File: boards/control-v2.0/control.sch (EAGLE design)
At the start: 107 parts, among them IC1 MCP23017-E/SS, J1 HFW8R-1ST, J2 B2PS-CENTERED-VH(LF)(SN), J3 SBH11-PBPC-D05-RA, J9 DF22-2, U1 TLV70233DBVR, U3 VND5E006ASPTR-E, U4 LMZ14201, U5 MCP1824T-1202E/OT, U6 MCP1824T-2502E/OT, X1 ASV-18.432MHZ-EJ-T

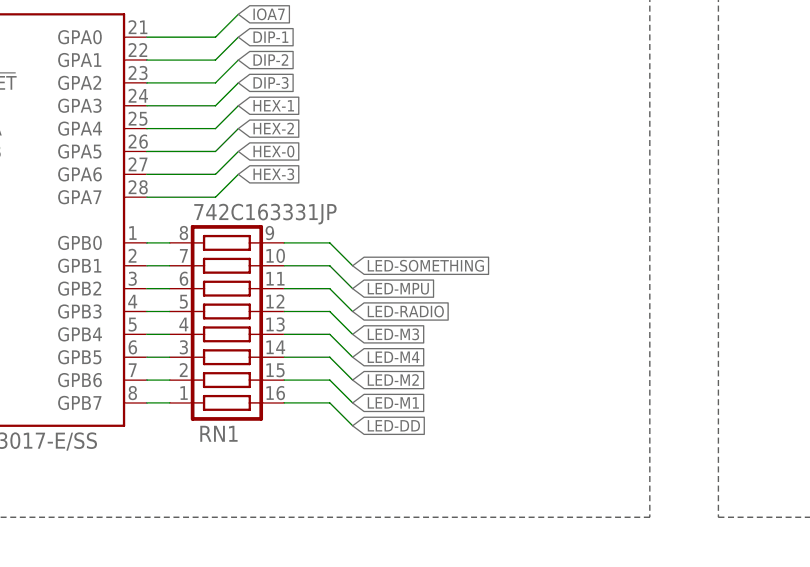
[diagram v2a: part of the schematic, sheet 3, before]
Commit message: Control technically no airwires and passes DRC
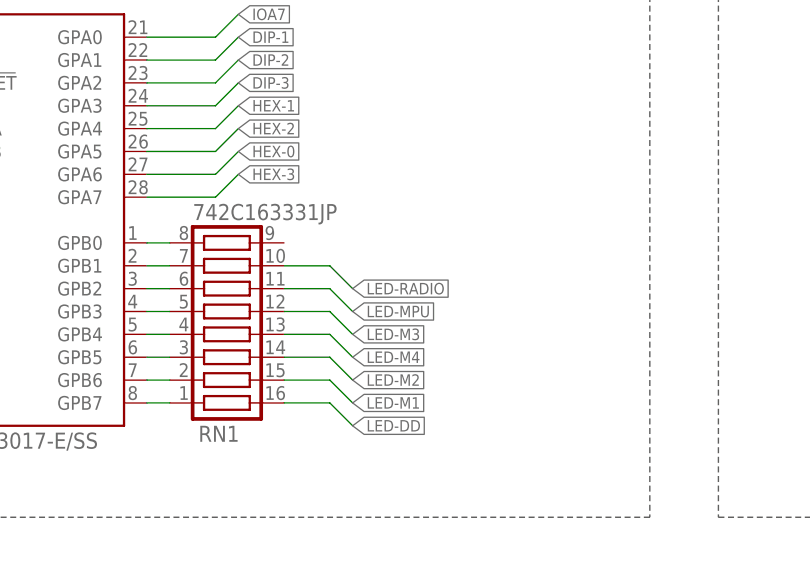
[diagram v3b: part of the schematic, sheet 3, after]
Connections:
- removed net LED-SOMETHING: RN1.9
- net LED-MPU: now also RN1.11; no longer RN1.10
- net LED-RADIO: now also RN1.10; no longer RN1.11
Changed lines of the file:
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@@
 <net name="LED-RADIO" class="0">
+<segment>
+<pinref part="D9" gate="G$1" pin="K"/>
+<wire x1="226.06" y1="172.72" x2="223.52" y2="172.72" width="0.1524" layer="91"/>
+<label x="223.52" y="172.72" size="1.27" layer="95" rot="R180" xref="yes"/>
+</segment>
+<segment>
+<wire x1="93.98" y1="162.56" x2="96.52" y2="160.02" width="0.1524" layer="91"/>
+<label x="96.52" y="160.02" size="1.27" layer="95" xref="yes"/>
+<pinref part="RN1" gate="G$1" pin="10"/>
+<wire x1="88.9" y1="162.56" x2="93.98" y2="162.56" width="0.1524" layer="91"/>
+</segment>
+</net>
+<net name="LED-DD" class="0">
+<segment>
+<wire x1="93.98" y1="147.32" x2="96.52" y2="144.78" width="0.1524" layer="91"/>
+<label x="96.52" y="144.78" size="1.27" layer="95" xref="yes"/>
+<pinref part="RN1" gate="G$1" pin="16"/>
+<wire x1="88.9" y1="147.32" x2="93.98" y2="147.32" width="0.1524" layer="91"/>
+</segment>
+</net>
+<net name="LED-MPU" class="0">
+<segment>
+<pinref part="D10" gate="G$1" pin="K"/>
+<wire x1="38.1" y1="114.3" x2="40.64" y2="114.3" width="0.1524" layer="91"/>
+<label x="40.64" y="114.3" size="1.27" layer="95" xref="yes"/>
+</segment>
 <segment>
 <wire x1="93.98" y1="160.02" x2="96.52" y2="157.48" width="0.1524" layer="91"/>
@@
 <pinref part="RN1" gate="G$1" pin="11"/>
 <wire x1="88.9" y1="160.02" x2="93.98" y2="160.02" width="0.1524" layer="91"/>
-</segment>
-<segment>
-<pinref part="D9" gate="G$1" pin="K"/>
-<wire x1="226.06" y1="172.72" x2="223.52" y2="172.72" width="0.1524" layer="91"/>
-<label x="223.52" y="172.72" size="1.27" layer="95" rot="R180" xref="yes"/>
-</segment>
-</net>
-<net name="LED-DD" class="0">
-<segment>
-<wire x1="93.98" y1="147.32" x2="96.52" y2="144.78" width="0.1524" layer="91"/>
-<label x="96.52" y="144.78" size="1.27" layer="95" xref="yes"/>
-<pinref part="RN1" gate="G$1" pin="16"/>
-<wire x1="88.9" y1="147.32" x2="93.98" y2="147.32" width="0.1524" layer="91"/>
-</segment>
-</net>
-<net name="LED-MPU" class="0">
-<segment>
-<pinref part="D10" gate="G$1" pin="K"/>
-<wire x1="38.1" y1="114.3" x2="40.64" y2="114.3" width="0.1524" layer="91"/>
-<label x="40.64" y="114.3" size="1.27" layer="95" xref="yes"/>
-</segment>
-<segment>
-<wire x1="93.98" y1="162.56" x2="96.52" y2="160.02" width="0.1524" layer="91"/>
-<label x="96.52" y="160.02" size="1.27" layer="95" xref="yes"/>
-<pinref part="RN1" gate="G$1" pin="10"/>
-<wire x1="88.9" y1="162.56" x2="93.98" y2="162.56" width="0.1524" layer="91"/>
 </segment>
 </net>
@@
 </segment>
 </net>
-<net name="LED-SOMETHING" class="0">
-<segment>
-<wire x1="93.98" y1="165.1" x2="96.52" y2="162.56" width="0.1524" layer="91"/>
-<label x="96.52" y="162.56" size="1.27" layer="95" xref="yes"/>
-<pinref part="RN1" gate="G$1" pin="9"/>
-<wire x1="88.9" y1="165.1" x2="93.98" y2="165.1" width="0.1524" layer="91"/>
-</segment>
-</net>

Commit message: Control switch layers, minor changes
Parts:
- SB1, SB2, SB3, SB4: value (none) -> SOLDERBRIDGESB0603
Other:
- moved on the sheet: C16, C17, C18, C19, C20, C21, C22, C23, C24, C25, C26, C27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

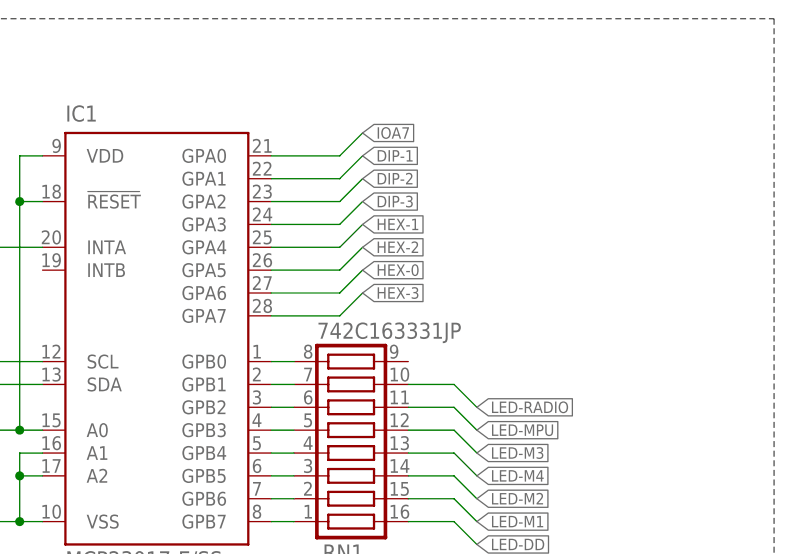
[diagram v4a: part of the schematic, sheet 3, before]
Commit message: Some clean up, smaller board
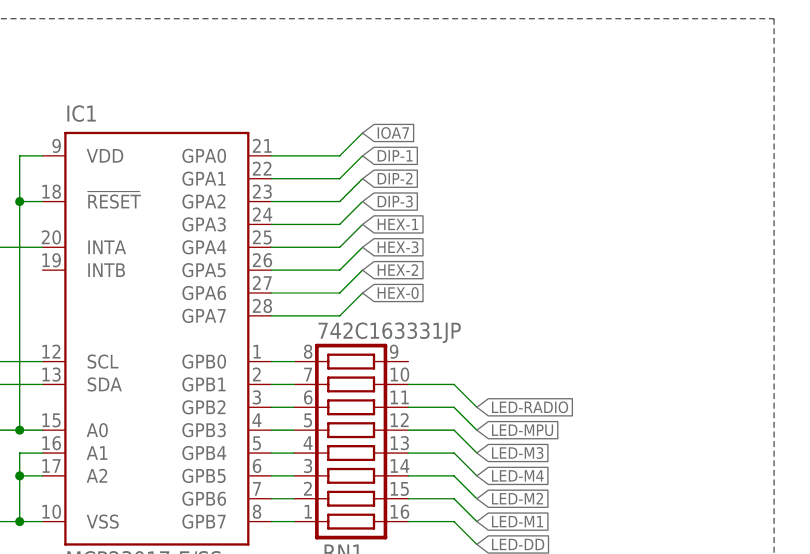
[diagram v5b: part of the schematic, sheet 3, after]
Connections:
- net +5V: now also J2.4; no longer U$1.4
- net ENC-A: now also J2.2; no longer J1G$1.2
- net ENC-B: now also J2.1; no longer J1G$1.1
- net GND: now also J1G$1.2, J2.3; no longer U$1.2
- net H1: now also J1G$1.1; no longer U$1.1
- net H2: now also J1G$1.3; no longer U$1.3
- net H3: now also J1G$1.5; no longer U$1.5
- net HEX-0: now also IC1.GPA7; no longer IC1.GPA6
- net HEX-2: now also IC1.GPA6; no longer IC1.GPA5
- net HEX-3: now also IC1.GPA5; no longer IC1.GPA7
- net PHASE-A: now also J1G$1.7; no longer U$1.7
- net PHASE-B: now also J1G$1.8; no longer U$1.8
- net PHASE-C: no longer U$1.6
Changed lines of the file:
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@@
 <part name="GND12" library="supply1" deviceset="GND" device=""/>
 <part name="SUPPLY1" library="supply2" deviceset="+5V" device=""/>
-<part name="U$1" library="RoboJackets-Connectors" deviceset="MKS-1658" device=""/>
-<part name="J1" library="RoboJackets-Connectors" deviceset="4-PIN_2MM-*" device="H"/>
+<part name="J1" library="RoboJackets-Connectors" deviceset="MKS-1658" device=""/>
+<part name="J2" library="RoboJackets-Connectors" deviceset="4-PIN_2MM-*" device="H"/>
 </parts>
 <sheets>
@@
 <instance part="GND12" gate="1" x="228.6" y="71.12"/>
 <instance part="SUPPLY1" gate="+5V" x="231.14" y="119.38"/>
-<instance part="U$1" gate="G$1" x="256.54" y="88.9" rot="MR180"/>
-<instance part="J1" gate="G$1" x="254" y="109.22" rot="R180"/>
+<instance part="J1" gate="G$1" x="254" y="88.9" rot="MR180"/>
+<instance part="J2" gate="G$1" x="254" y="109.22" rot="R180"/>
 </instances>
 <busses>
@@
 <wire x1="246.38" y1="93.98" x2="243.84" y2="93.98" width="0.1524" layer="91"/>
 <label x="243.84" y="93.98" size="1.27" layer="95" rot="R180" xref="yes"/>
-<pinref part="U$1" gate="G$1" pin="7"/>
+<pinref part="J1" gate="G$1" pin="7"/>
 </segment>
 <segment>
@@
 <wire x1="246.38" y1="96.52" x2="243.84" y2="96.52" width="0.1524" layer="91"/>
 <label x="243.84" y="96.52" size="1.27" layer="95" rot="R180" xref="yes"/>
-<pinref part="U$1" gate="G$1" pin="8"/>
+<pinref part="J1" gate="G$1" pin="8"/>
 </segment>
 <segment>
@@
 <wire x1="246.38" y1="91.44" x2="243.84" y2="91.44" width="0.1524" layer="91"/>
 <label x="243.84" y="91.44" size="1.27" layer="95" rot="R180" xref="yes"/>
-<pinref part="U$1" gate="G$1" pin="6"/>
+<pinref part="J1" gate="G$1" pin="6"/>
 </segment>
 </net>
@@
 <wire x1="228.6" y1="73.66" x2="228.6" y2="81.28" width="0.1524" layer="91"/>
 <junction x="228.6" y="81.28"/>
-<pinref part="U$1" gate="G$1" pin="2"/>
-<pinref part="J1" gate="G$1" pin="3"/>
+<pinref part="J1" gate="G$1" pin="2"/>
+<pinref part="J2" gate="G$1" pin="3"/>
 </segment>
 </net>
@@
 <wire x1="246.38" y1="78.74" x2="243.84" y2="78.74" width="0.1524" layer="91"/>
 <label x="243.84" y="78.74" size="1.27" layer="95" rot="R180" xref="yes"/>
-<pinref part="U$1" gate="G$1" pin="1"/>
+<pinref part="J1" gate="G$1" pin="1"/>
 </segment>
 </net>
@@
 <wire x1="246.38" y1="83.82" x2="243.84" y2="83.82" width="0.1524" layer="91"/>
 <label x="243.84" y="83.82" size="1.27" layer="95" rot="R180" xref="yes"/>
-<pinref part="U$1" gate="G$1" pin="3"/>
+<pinref part="J1" gate="G$1" pin="3"/>
 </segment>
 </net>
@@
 <wire x1="246.38" y1="88.9" x2="243.84" y2="88.9" width="0.1524" layer="91"/>
 <label x="243.84" y="88.9" size="1.27" layer="95" rot="R180" xref="yes"/>
-<pinref part="U$1" gate="G$1" pin="5"/>
+<pinref part="J1" gate="G$1" pin="5"/>
 </segment>
 </net>
@@
 <wire x1="246.38" y1="111.76" x2="248.92" y2="111.76" width="0.1524" layer="91"/>
 <label x="246.38" y="111.76" size="1.27" layer="95" rot="R180" xref="yes"/>
-<pinref part="J1" gate="G$1" pin="2"/>
+<pinref part="J2" gate="G$1" pin="2"/>
 </segment>
 </net>
@@
 <wire x1="246.38" y1="109.22" x2="248.92" y2="109.22" width="0.1524" layer="91"/>
 <label x="246.38" y="109.22" size="1.27" layer="95" rot="R180" xref="yes"/>
-<pinref part="J1" gate="G$1" pin="1"/>
+<pinref part="J2" gate="G$1" pin="1"/>
 </segment>
 </net>
@@
 <junction x="231.14" y="116.84"/>
 <wire x1="246.38" y1="116.84" x2="248.92" y2="116.84" width="0.1524" layer="91"/>
-<pinref part="U$1" gate="G$1" pin="4"/>
 <pinref part="J1" gate="G$1" pin="4"/>
+<pinref part="J2" gate="G$1" pin="4"/>
 </segment>
 </net>
@@
 <net name="HEX-0" class="0">
 <segment>
-<pinref part="IC1" gate="G$1" pin="GPA6"/>
-<wire x1="73.66" y1="172.72" x2="81.28" y2="172.72" width="0.1524" layer="91"/>
-<wire x1="81.28" y1="172.72" x2="83.82" y2="175.26" width="0.1524" layer="91"/>
-<label x="83.82" y="175.26" size="1.27" layer="95" xref="yes"/>
-</segment>
-<segment>
 <pinref part="S2" gate="G$1" pin="1"/>
 <wire x1="170.18" y1="187.96" x2="172.72" y2="187.96" width="0.1524" layer="91"/>
 <label x="172.72" y="187.96" size="1.27" layer="95" xref="yes"/>
 </segment>
+<segment>
+<pinref part="IC1" gate="G$1" pin="GPA7"/>
+<wire x1="73.66" y1="170.18" x2="81.28" y2="170.18" width="0.1524" layer="91"/>
+<wire x1="81.28" y1="170.18" x2="83.82" y2="172.72" width="0.1524" layer="91"/>
+<label x="83.82" y="172.72" size="1.27" layer="95" xref="yes"/>
+</segment>
 </net>
 <net name="IOA7" class="0">
@@
 </segment>
 <segment>
-<pinref part="IC1" gate="G$1" pin="GPA7"/>
-<wire x1="73.66" y1="170.18" x2="81.28" y2="170.18" width="0.1524" layer="91"/>
-<wire x1="81.28" y1="170.18" x2="83.82" y2="172.72" width="0.1524" layer="91"/>
-<label x="83.82" y="172.72" size="1.27" layer="95" xref="yes"/>
+<pinref part="IC1" gate="G$1" pin="GPA5"/>
+<wire x1="73.66" y1="175.26" x2="81.28" y2="175.26" width="0.1524" layer="91"/>
+<wire x1="81.28" y1="175.26" x2="83.82" y2="177.8" width="0.1524" layer="91"/>
+<label x="83.82" y="177.8" size="1.27" layer="95" xref="yes"/>
 </segment>
 </net>
@@
 </segment>
 <segment>
-<pinref part="IC1" gate="G$1" pin="GPA5"/>
-<wire x1="73.66" y1="175.26" x2="81.28" y2="175.26" width="0.1524" layer="91"/>
-<wire x1="81.28" y1="175.26" x2="83.82" y2="177.8" width="0.1524" layer="91"/>
-<label x="83.82" y="177.8" size="1.27" layer="95" xref="yes"/>
+<pinref part="IC1" gate="G$1" pin="GPA6"/>
+<wire x1="73.66" y1="172.72" x2="81.28" y2="172.72" width="0.1524" layer="91"/>
+<wire x1="81.28" y1="172.72" x2="83.82" y2="175.26" width="0.1524" layer="91"/>
+<label x="83.82" y="175.26" size="1.27" layer="95" xref="yes"/>
 </segment>
 </net>
